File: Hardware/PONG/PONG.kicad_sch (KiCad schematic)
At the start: 7 parts, among them U1 74AHC04, U2 74LS73, Y1 Crystal

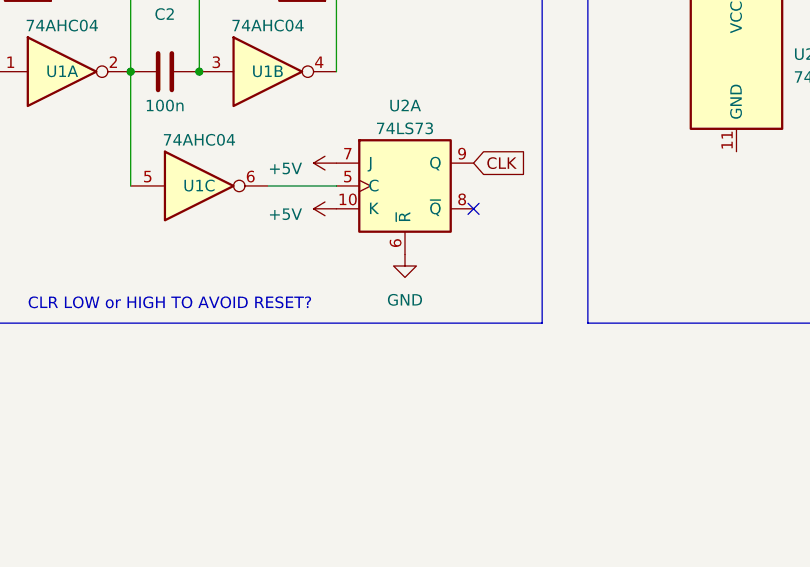
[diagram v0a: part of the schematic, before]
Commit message: added 5V to CLR pin to avoid reset and ensure stability
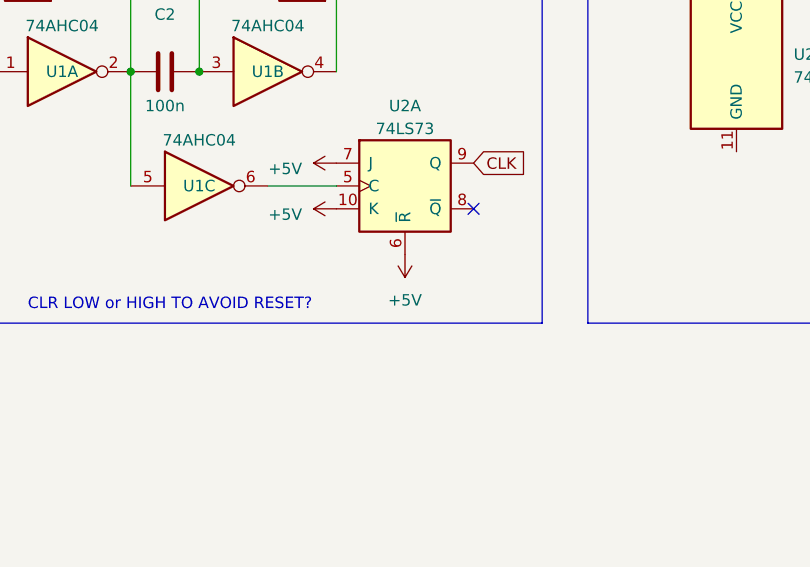
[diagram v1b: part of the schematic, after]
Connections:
- net GND is gone; now on net +5V: U2.6 (~{R})
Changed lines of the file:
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@@
+    )
+  )
+  (symbol (lib_id "power:+5V") (at 76.2 71.12 180) (unit 1)
+    (in_bom yes) (on_board yes) (dnp no) (fields_autoplaced)
+    (property "Reference" "#PWR03" (at 76.2 67.31 0)
+      (effects (font (size 1.27 1.27)) hide)
+    )
+    (property "Value" "+5V" (at 76.2 76.2 0)
+      (effects (font (size 1.27 1.27)))
+    )
+    (property "Footprint" "" (at 76.2 71.12 0)
+      (effects (font (size 1.27 1.27)) hide)
+    )
+    (property "Datasheet" "" (at 76.2 71.12 0)
+      (effects (font (size 1.27 1.27)) hide)
+    )
+    (pin "1")
+    (instances
+      (project "PONG"
+        (path "/f15d9fd0-247d-404e-8490-6de125b4aecb"
+          (reference "#PWR03") (unit 1)
+        )
+      )
     )
   )
@@
         )
       )
-    )
-  )
-  (symbol (lib_id "power:GND") (at 76.2 71.12 0) (unit 1)
-    (in_bom yes) (on_board yes) (dnp no) (fields_autoplaced)
-    (property "Reference" "#PWR03" (at 76.2 77.47 0)
-      (effects (font (size 1.27 1.27)) hide)
-    )
-    (property "Value" "GND" (at 76.2 76.2 0)
-      (effects (font (size 1.27 1.27)))
-    )
-    (property "Footprint" "" (at 76.2 71.12 0)
-      (effects (font (size 1.27 1.27)) hide)
-    )
-    (property "Datasheet" "" (at 76.2 71.12 0)
-      (effects (font (size 1.27 1.27)) hide)
-    )
-    (pin "1")
-    (instances
-      (project "PONG"
-        (path "/f15d9fd0-247d-404e-8490-6de125b4aecb"
-          (reference "#PWR03") (unit 1)
-        )
-      )

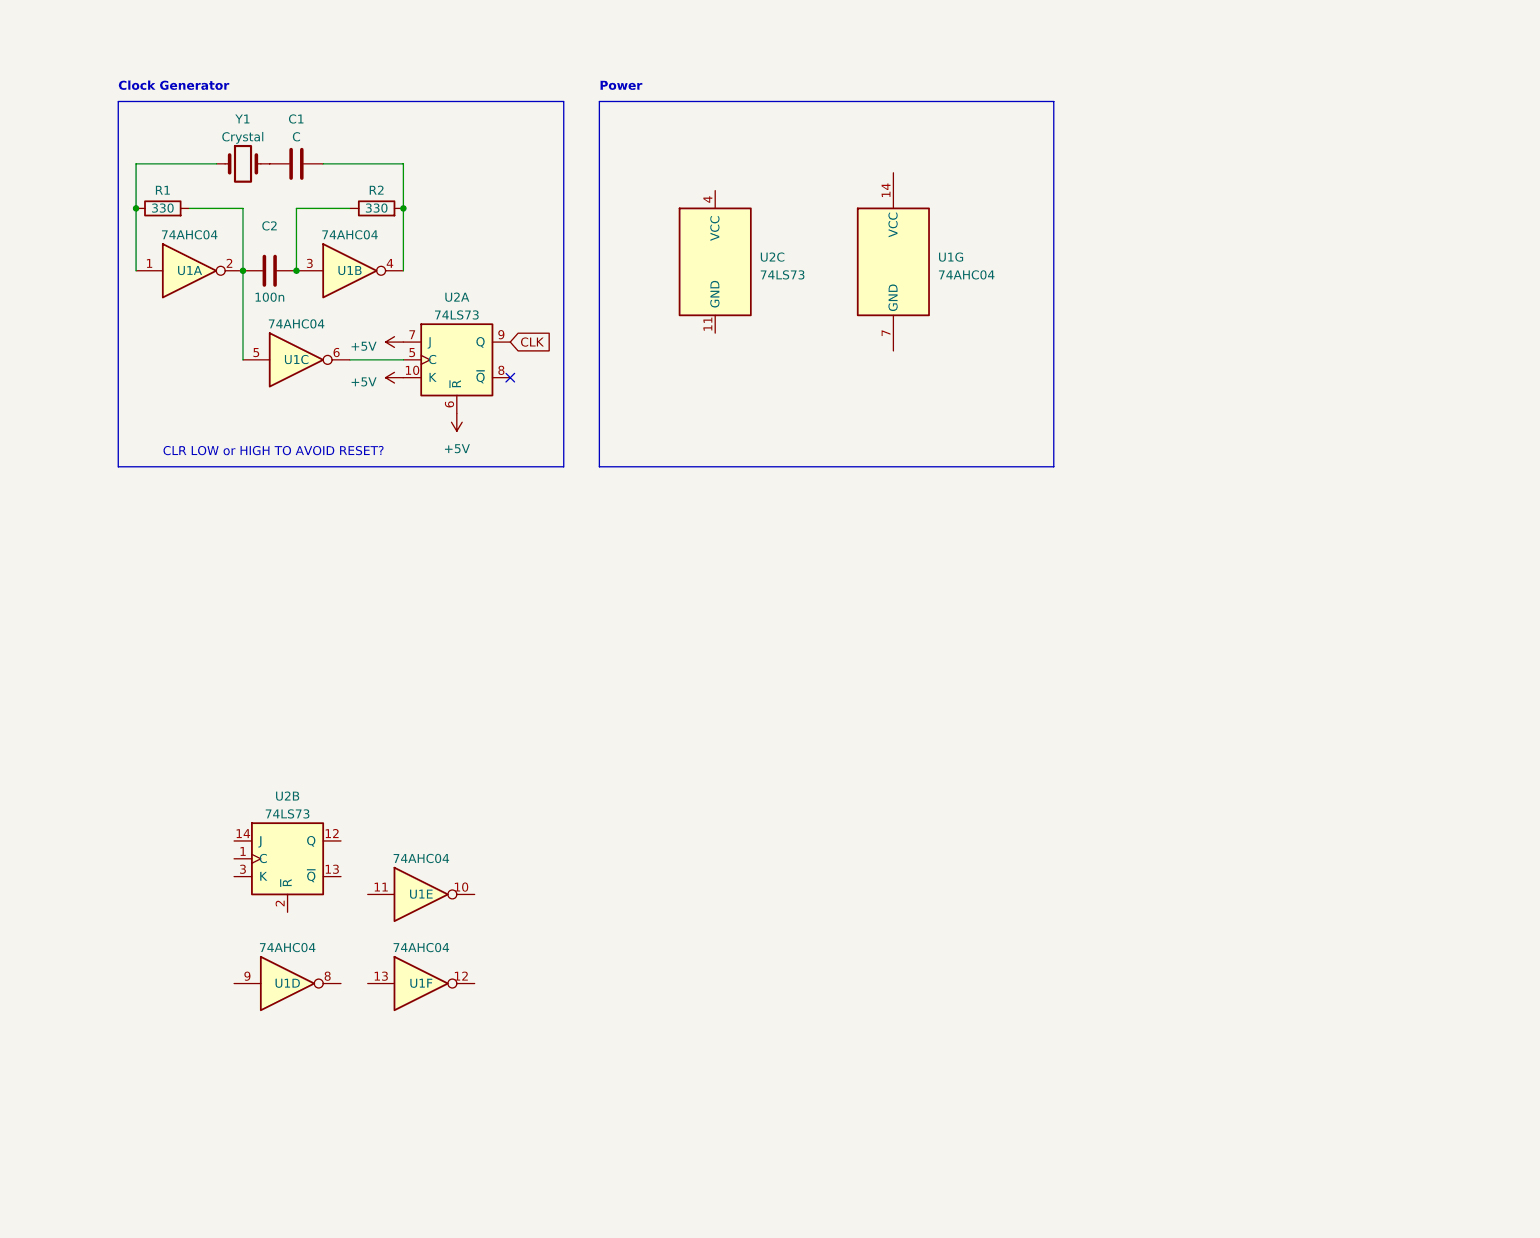
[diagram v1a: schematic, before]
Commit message: Laying out components, need to find how to control counter, also added circuitry for 5 inout NAND gate
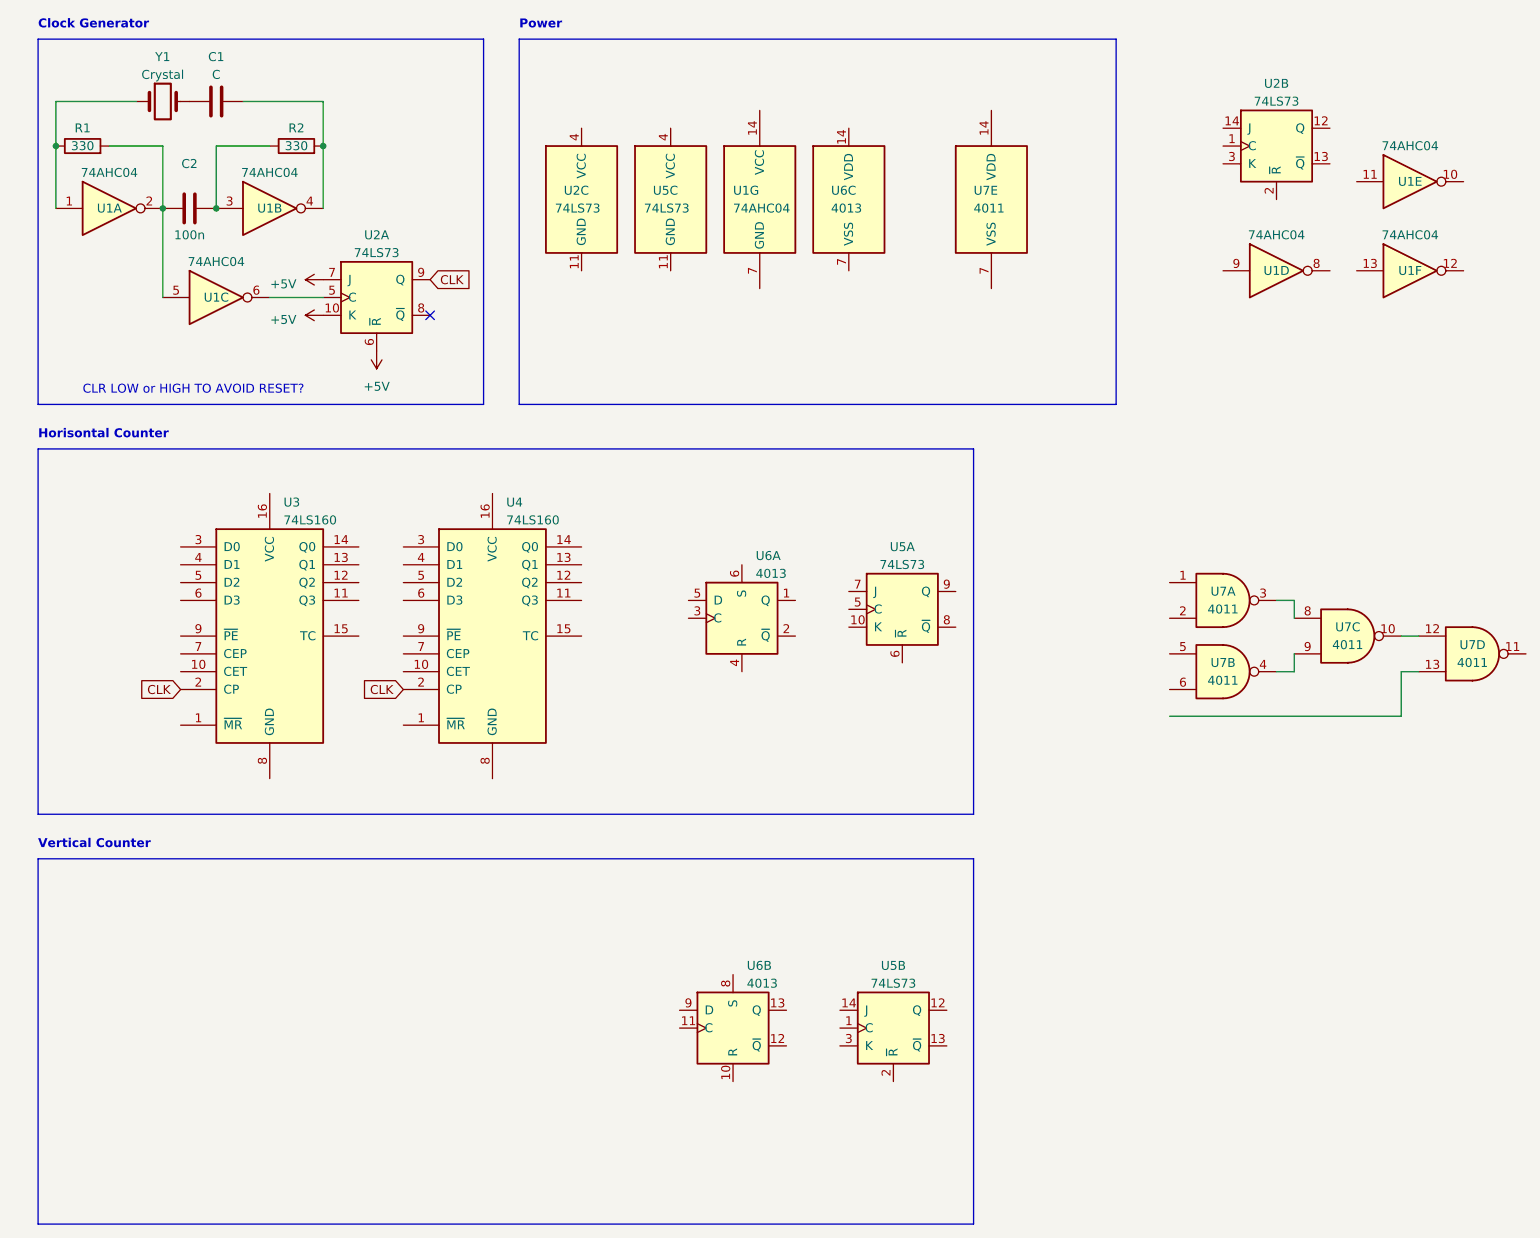
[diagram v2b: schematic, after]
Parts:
- added U3, U4: 74LS160, symbol 74xx:74LS160
- added U5: 74LS73, symbol 74xx:74LS73
- added U6: 4013, symbol 4xxx:4013
- added U7: 4011, symbol 4xxx:4011
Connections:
- net CLK: now also U3.2 (CP), U4.2 (CP)
- new net: U7.3, U7.8
- new net: U7.10, U7.12
- new net: U7.4, U7.9
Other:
- note added: "Horisontal Counter"
- note added: "Vertical Counter"
- moved on the sheet: C1, C2, R1, R2, U1A, U1B, U1C, U1D, U1E, U1F, U1G, U2A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

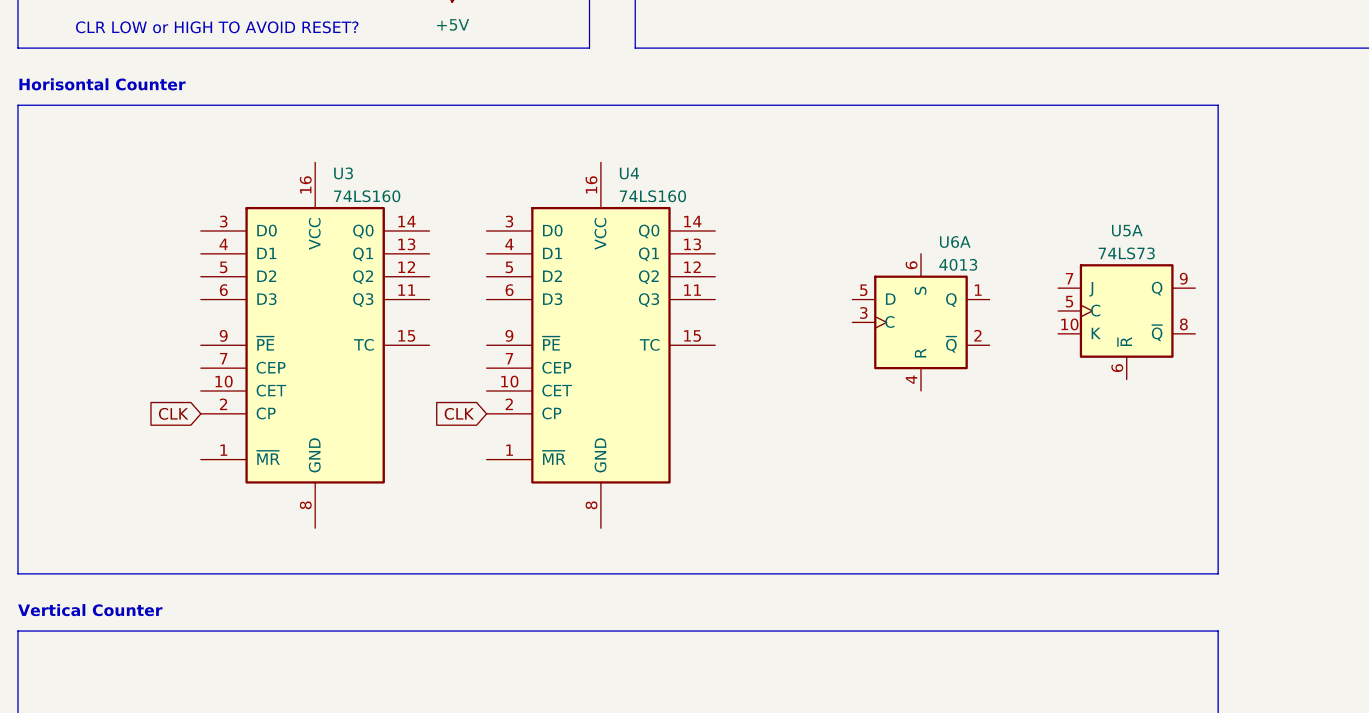
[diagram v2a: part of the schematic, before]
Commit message: switched from 74LS160 to 74LS161 because we want to count to 16 not 10
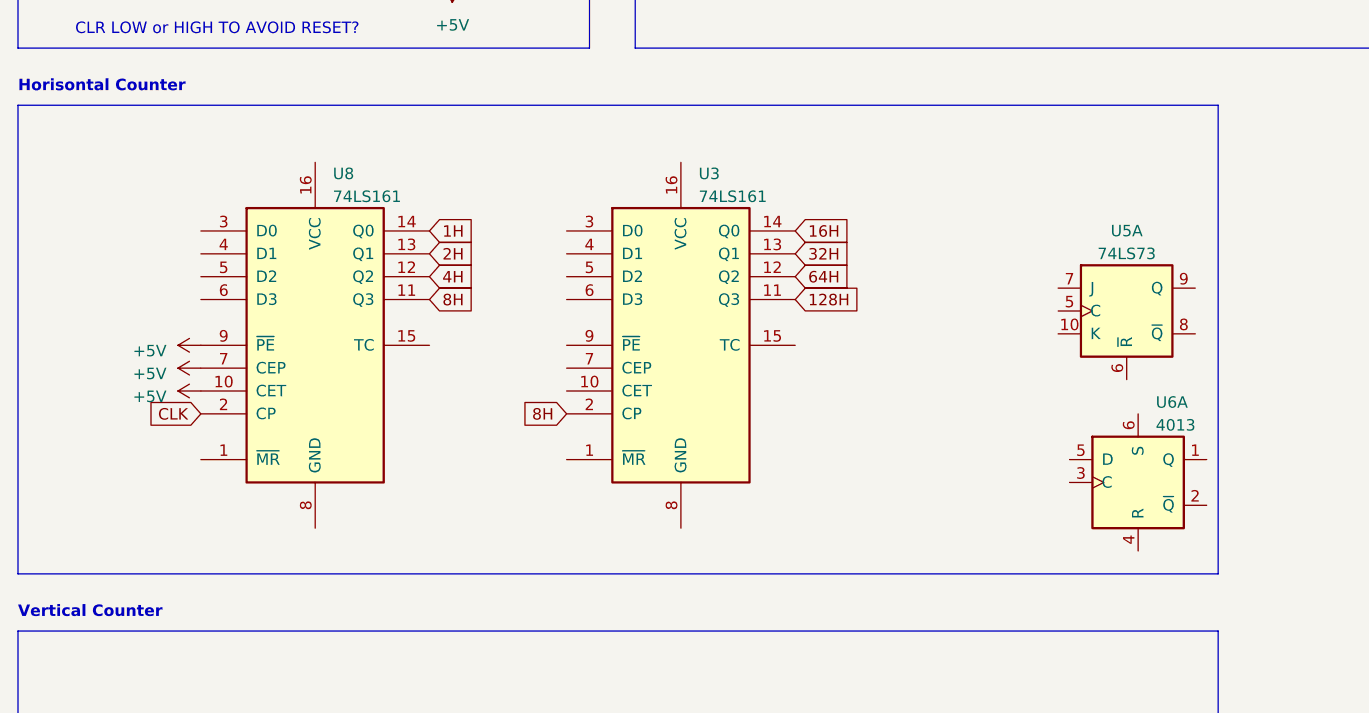
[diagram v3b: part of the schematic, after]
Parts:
- removed U3, U4: 74LS160, symbol 74xx:74LS160
- added U3, U8: 74LS161, symbol 74xx:74LS161
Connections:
- net +5V: now also U8.10 (CET), U8.7 (CEP), U8.9 (~{PE})
- net CLK: now also U8.2 (CP)
- new net 128H: U3.11 (Q3)
- new net 16H: U3.14 (Q0)
- new net 1H: U8.14 (Q0)
- new net 2H: U8.13 (Q1)
- new net 32H: U3.13 (Q1)
- new net 4H: U8.12 (Q2)
- new net 64H: U3.12 (Q2)
- new net 8H: U3.2 (CP), U8.11 (Q3)
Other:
- moved on the sheet: U6A

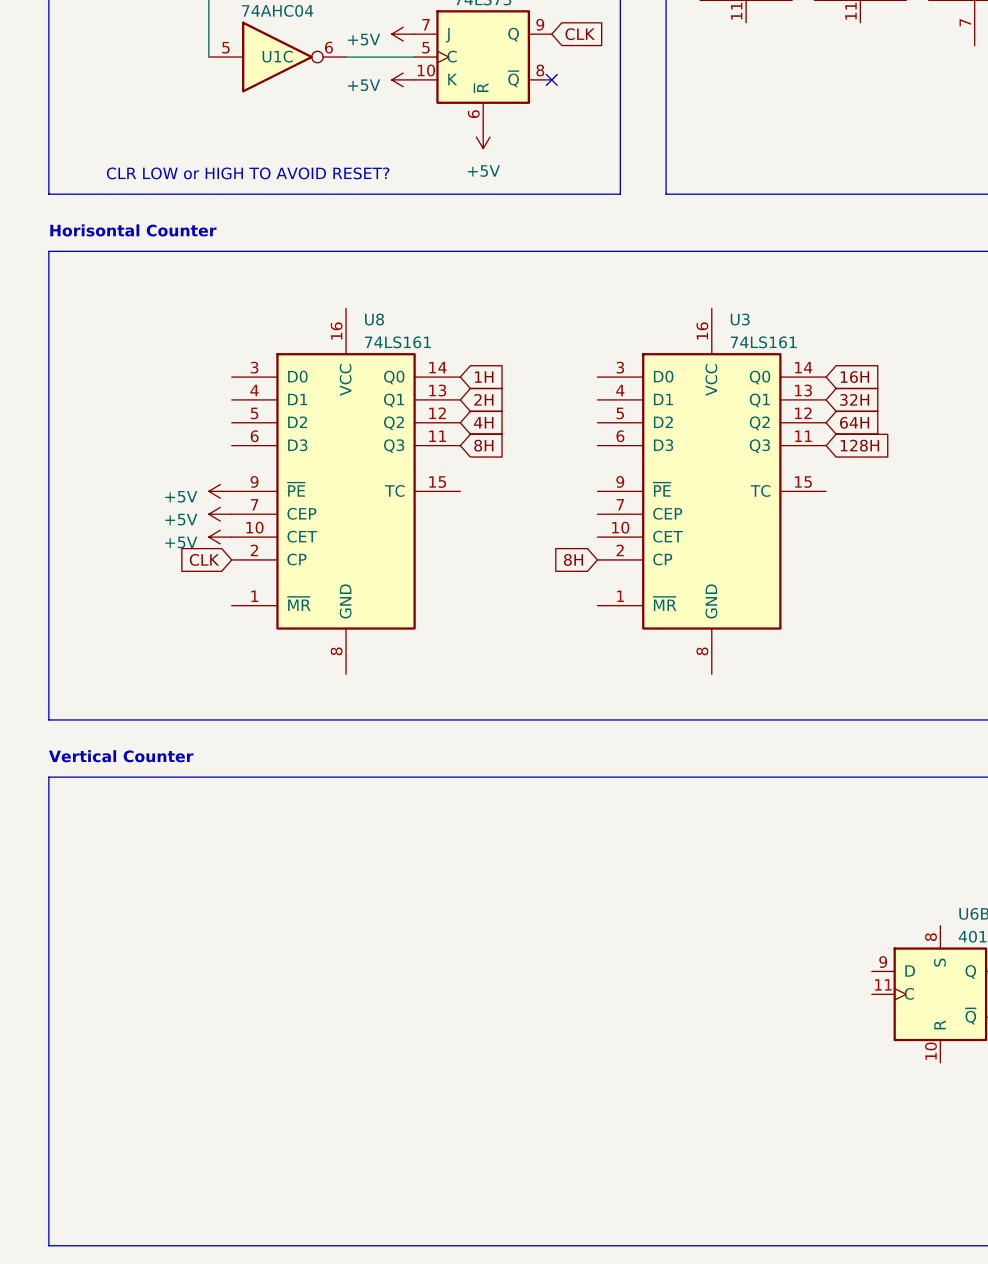
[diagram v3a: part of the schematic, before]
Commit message: Not sure what counter to use at the moment, trying to find the one with the least amount of pins
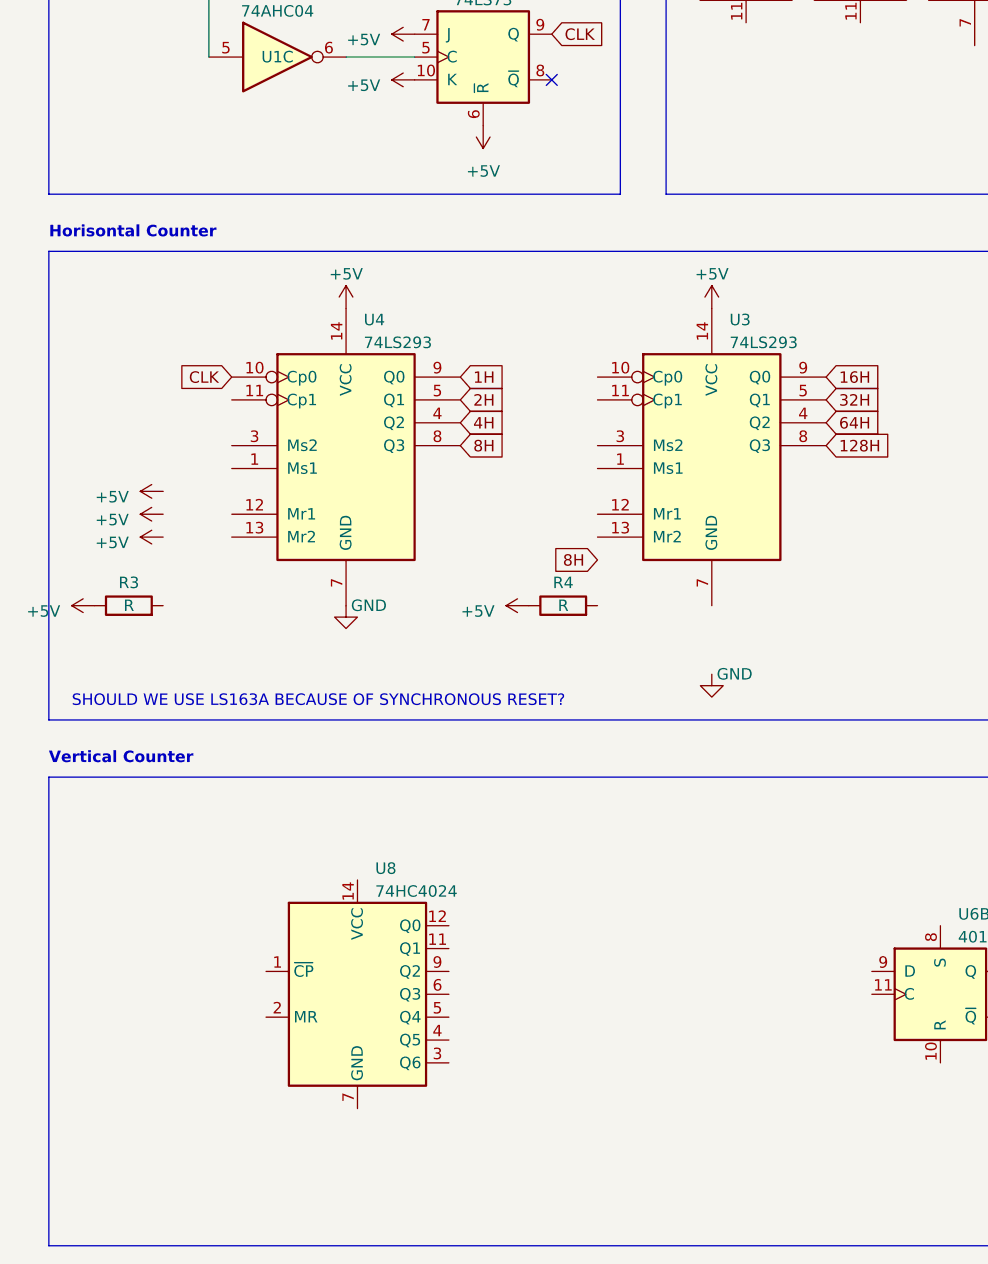
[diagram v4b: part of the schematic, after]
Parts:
- removed U3, U8: 74LS161, symbol 74xx:74LS161
- added R3, R4: R, symbol Device:R
- added U3, U4: 74LS293, symbol 74xx:74LS293
- added U8: 74HC4024, Package_SO:SOIC-14_3.9x8.7mm_P1.27mm, symbol 74xx:74HC4024
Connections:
- net +5V: now also R3.1, R4.1, U3.14 (VCC), U4.14 (VCC)
- net 128H: now also U3.8 (Q3)
- net 16H: now also U3.9 (Q0)
- net 1H: now also U4.9 (Q0)
- net 2H: now also U4.5 (Q1)
- net 32H: now also U3.5 (Q1)
- net 4H: now also U4.4 (Q2)
- net 64H: now also U3.4 (Q2)
- net 8H: now also U4.8 (Q3)
- net CLK: now also U4.10 (Cp0)
- new net GND: U4.7 (GND)
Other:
- note added: "SHOULD WE USE LS163A BECAUSE OF SYNCHRONOUS RESET?"
- note removed: "CLR LOW or HIGH TO AVOID RESET?"
